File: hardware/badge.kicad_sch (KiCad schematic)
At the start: 0 parts

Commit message: add lcd sch
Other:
- added sheet lcd (lcd.kicad_sch)
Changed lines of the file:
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@@
+	)
+	(sheet
+		(at 162.56 46.99)
+		(size 29.21 26.67)
+		(fields_autoplaced yes)
+		(stroke
+			(width 0.1524)
+			(type solid)
+		)
+		(fill
+			(color 0 0 0 0.0000)
+		)
+		(property "Sheetname" "lcd"
+			(at 162.56 46.2784 0)
+			(effects
+				(font
+					(size 1.27 1.27)
+				)
+				(justify left bottom)
+			)
+		)
+		(property "Sheetfile" "lcd.kicad_sch"
+			(at 162.56 74.2446 0)
+			(effects
+				(font
+					(size 1.27 1.27)
+				)
+				(justify left top)
+			)
+		)
+		(instances
+			(project "badge"
+				(path "/dc4a3d77-b0f8-4e90-a4be-3e93c7025348"
+					(page "6")
+				)
+			)
+		)
 	)
 	(sheet

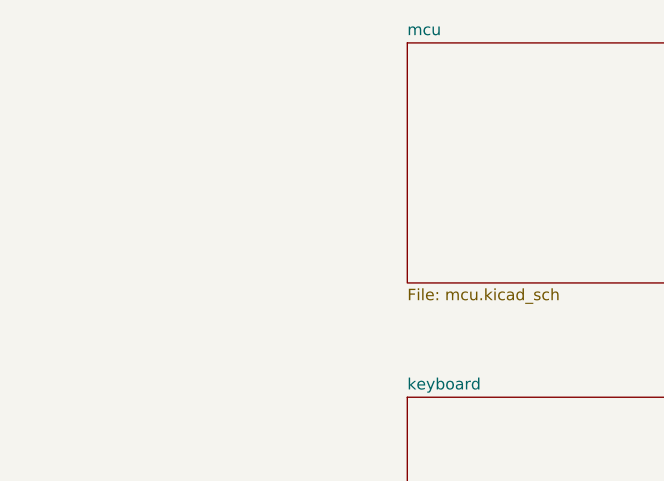
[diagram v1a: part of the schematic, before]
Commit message: remove ch340
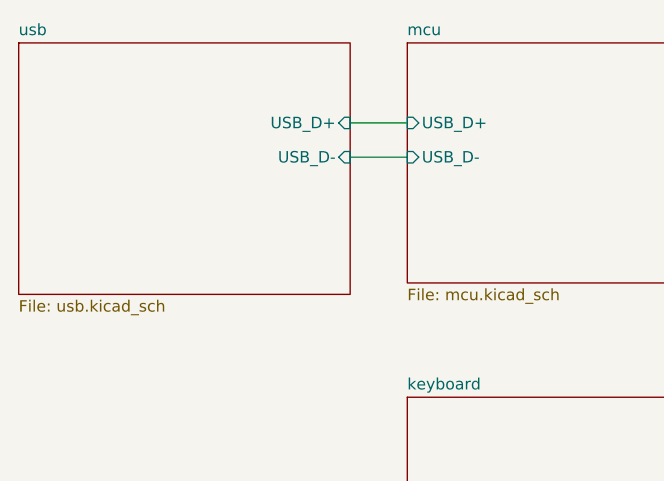
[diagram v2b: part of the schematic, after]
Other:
- added sheet usb (usb.kicad_sch)
- sheet mcu ports: added USB_D+, USB_D-; removed none
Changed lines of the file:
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@@
 	(generator_version "8.0")
 	(paper "A4")
+	(wire
+		(pts
+			(xy 71.12 59.69) (xy 77.47 59.69)
+		)
+		(stroke
+			(width 0)
+			(type default)
+		)
+	)
+	(wire
+		(pts
+			(xy 71.12 55.88) (xy 77.47 55.88)
+		)
+		(stroke
+			(width 0)
+			(type default)
+		)
+	)
+	(sheet
+		(at 34.29 46.99)
+		(size 36.83 27.94)
+		(fields_autoplaced yes)
+		(stroke
+			(width 0.1524)
+			(type solid)
+		)
+		(fill
+			(color 0 0 0 0.0000)
+		)
+		(property "Sheetname" "usb"
+			(at 34.29 46.2784 0)
+			(effects
+				(font
+					(size 1.27 1.27)
+				)
+				(justify left bottom)
+			)
+		)
+		(property "Sheetfile" "usb.kicad_sch"
+			(at 34.29 75.5146 0)
+			(effects
+				(font
+					(size 1.27 1.27)
+				)
+				(justify left top)
+			)
+		)
+		(pin "USB_D+" input
+			(at 71.12 55.88 0)
+			(effects
+				(font
+					(size 1.27 1.27)
+				)
+				(justify right)
+			)
+		)
+		(pin "USB_D-" input
+			(at 71.12 59.69 0)
+			(effects
+				(font
+					(size 1.27 1.27)
+				)
+				(justify right)
+			)
+		)
+		(instances
+			(project "badge"
+				(path "/dc4a3d77-b0f8-4e90-a4be-3e93c7025348"
+					(page "7")
+				)
+			)
+		)
+	)
 	(sheet
 		(at 77.47 86.36)
@@
 			)
 		)
+		(pin "USB_D+" input
+			(at 77.47 55.88 180)
+			(effects
+				(font
+					(size 1.27 1.27)
+				)
+				(justify left)
+			)
+		)
+		(pin "USB_D-" input
+			(at 77.47 59.69 180)
+			(effects
+				(font
+					(size 1.27 1.27)
+				)
+				(justify left)
+			)
+		)

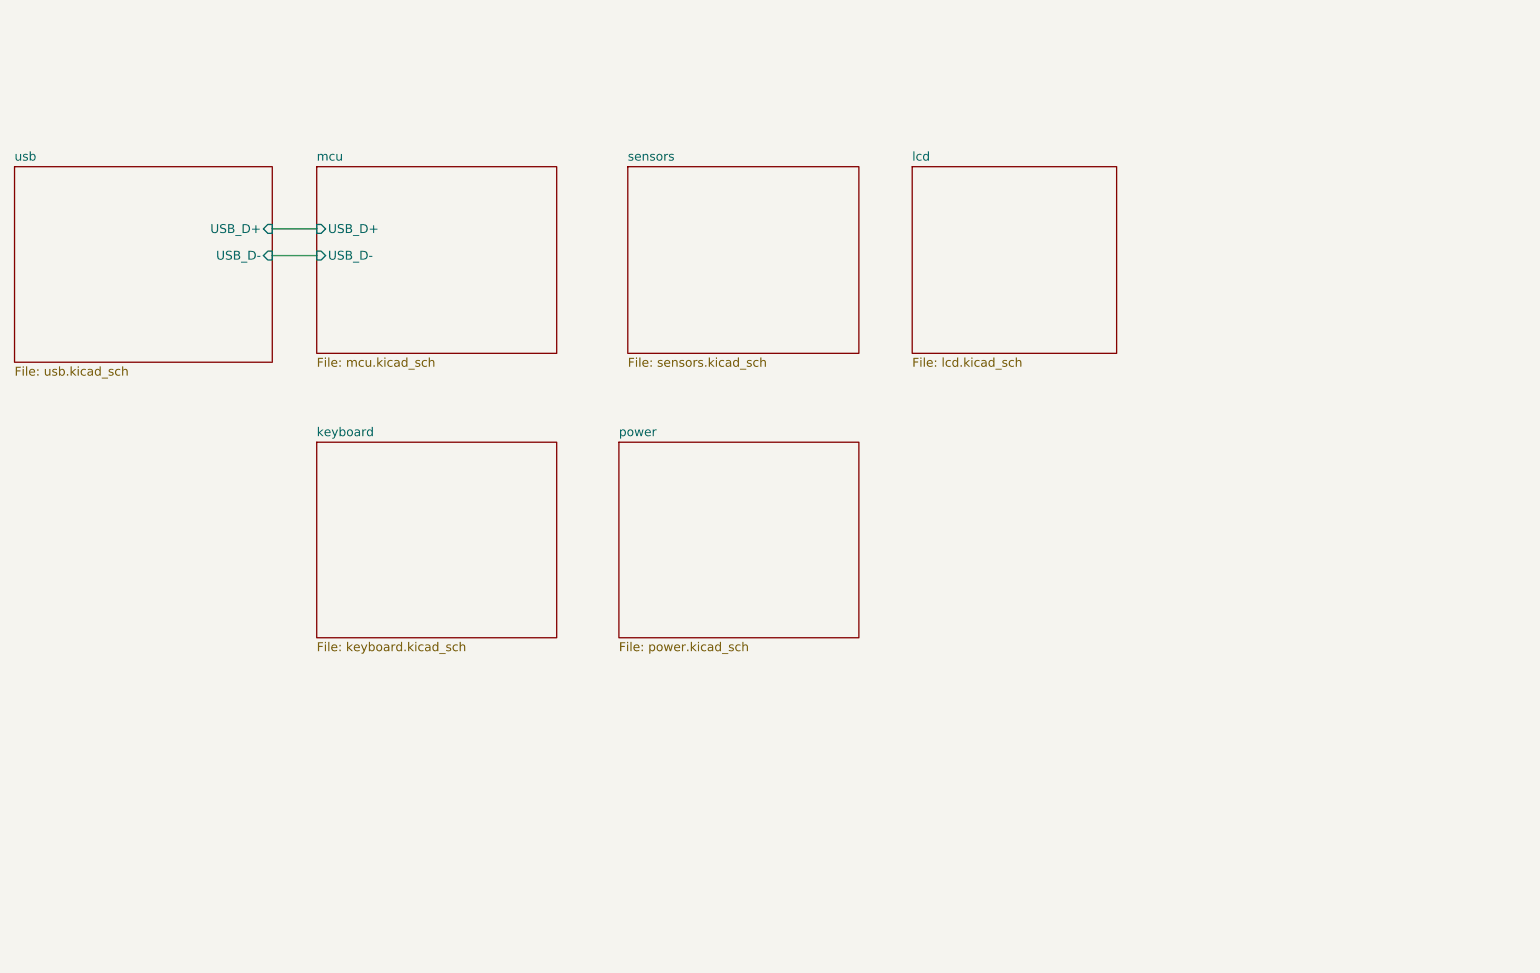
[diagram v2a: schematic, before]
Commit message: remove global labels
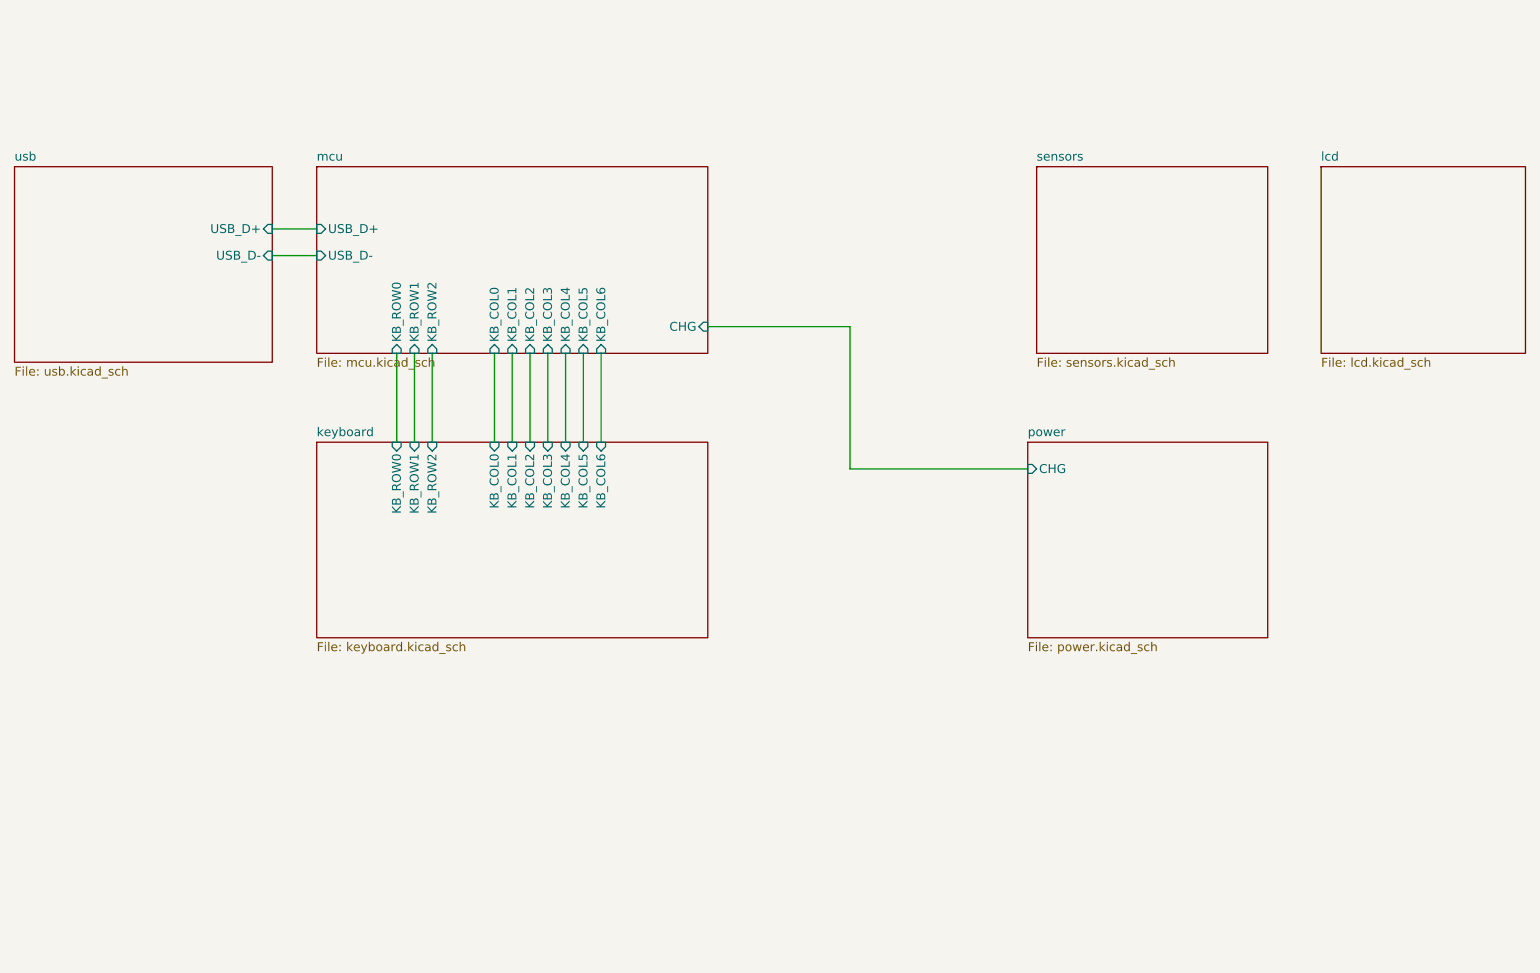
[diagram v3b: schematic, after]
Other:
- sheet keyboard ports: added KB_COL0, KB_COL1, KB_COL2, KB_COL3, KB_COL4, KB_COL5, KB_COL6, KB_ROW0, KB_ROW1, KB_ROW2; removed none
- sheet mcu ports: added CHG, KB_COL0, KB_COL1, KB_COL2, KB_COL3, KB_COL4, KB_COL5, KB_COL6, KB_ROW0, KB_ROW1, KB_ROW2; removed none
- sheet power ports: added CHG; removed none

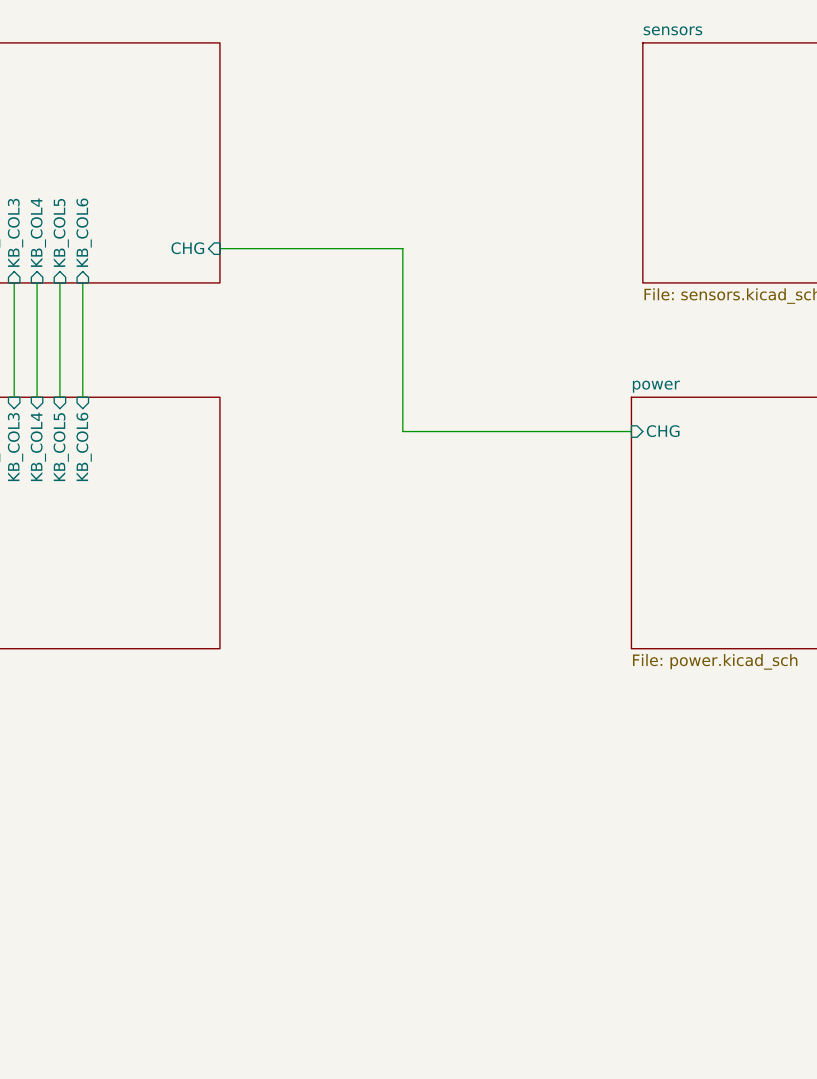
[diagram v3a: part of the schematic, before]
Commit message: add imu BMI270
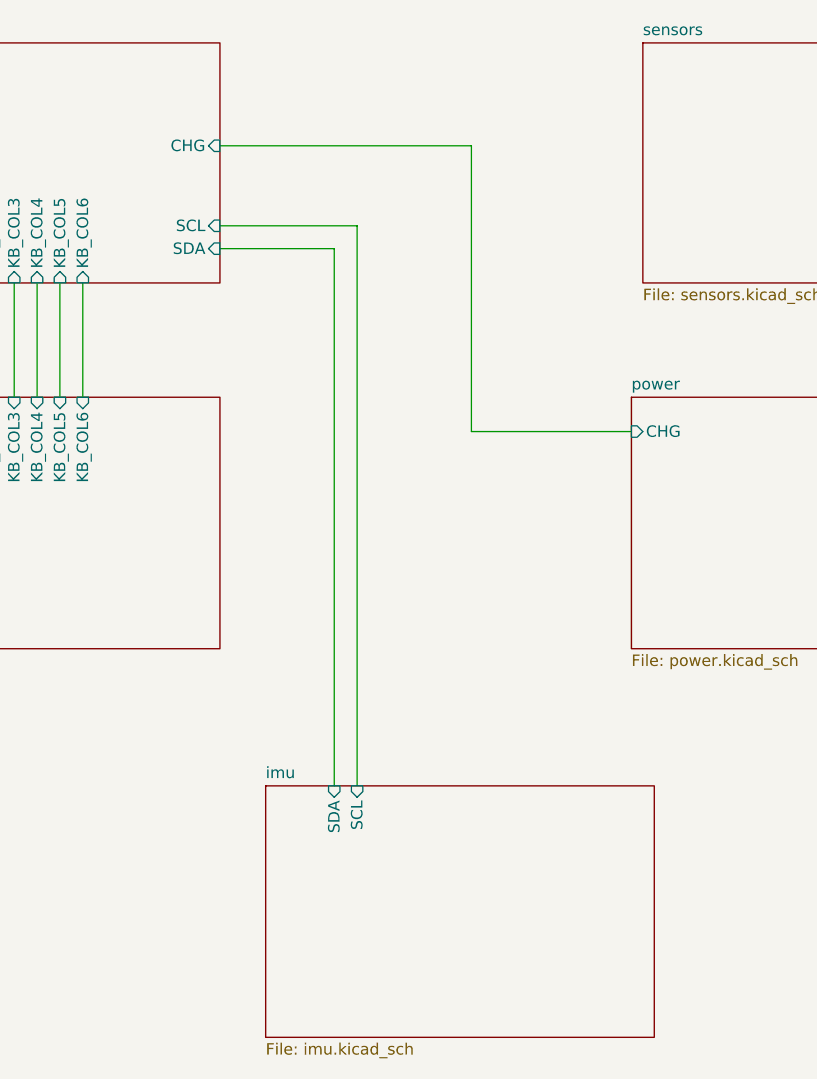
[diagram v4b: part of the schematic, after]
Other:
- added sheet imu (imu.kicad_sch)
- sheet mcu ports: added SCL, SDA; removed none
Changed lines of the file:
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@@
+	(wire
+		(pts
+			(xy 146.05 69.85) (xy 146.05 129.54)
+		)
+		(stroke
+			(width 0)
+			(type default)
+		)
+	)
 	(wire
 		(pts
@@
 	(wire
 		(pts
+			(xy 133.35 69.85) (xy 146.05 69.85)
+		)
+		(stroke
+			(width 0)
+			(type default)
+		)
+	)
+	(wire
+		(pts
+			(xy 148.59 67.31) (xy 148.59 129.54)
+		)
+		(stroke
+			(width 0)
+			(type default)
+		)
+	)
+	(wire
+		(pts
 			(xy 88.9 73.66) (xy 88.9 86.36)
 		)
@@
 	(wire
 		(pts
-			(xy 133.35 69.85) (xy 153.67 69.85)
+			(xy 133.35 67.31) (xy 148.59 67.31)
+		)
+		(stroke
+			(width 0)
+			(type default)
+		)
+	)
+	(wire
+		(pts
+			(xy 133.35 58.42) (xy 161.29 58.42)
 		)
 		(stroke
@@
 	(wire
 		(pts
-			(xy 153.67 90.17) (xy 179.07 90.17)
+			(xy 161.29 90.17) (xy 179.07 90.17)
 		)
 		(stroke
@@
 	(wire
 		(pts
-			(xy 153.67 69.85) (xy 153.67 90.17)
-		)
-		(stroke
-			(width 0)
-			(type default)
+			(xy 161.29 58.42) (xy 161.29 90.17)
+		)
+		(stroke
+			(width 0)
+			(type default)
+		)
+	)
+	(sheet
+		(at 138.43 129.54)
+		(size 43.18 27.94)
+		(fields_autoplaced yes)
+		(stroke
+			(width 0.1524)
+			(type solid)
+		)
+		(fill
+			(color 0 0 0 0.0000)
+		)
+		(property "Sheetname" "imu"
+			(at 138.43 128.8284 0)
+			(effects
+				(font
+					(size 1.27 1.27)
+				)
+				(justify left bottom)
+			)
+		)
+		(property "Sheetfile" "imu.kicad_sch"
+			(at 138.43 158.0646 0)
+			(effects
+				(font
+					(size 1.27 1.27)
+				)
+				(justify left top)
+			)
+		)
+		(pin "SDA" input
+			(at 146.05 129.54 90)
+			(effects
+				(font
+					(size 1.27 1.27)
+				)
+				(justify right)
+			)
+		)
+		(pin "SCL" input
+			(at 148.59 129.54 90)
+			(effects
+				(font
+					(size 1.27 1.27)
+				)
+				(justify right)
+			)
+		)
+		(instances
+			(project "badge"
+				(path "/dc4a3d77-b0f8-4e90-a4be-3e93c7025348"
+					(page "8")
+				)
+			)
 		)
 	)
@@
 		)
 		(pin "CHG" input
+			(at 133.35 58.42 0)
+			(effects
+				(font
+					(size 1.27 1.27)
+				)
+				(justify right)
+			)
+		)
+		(pin "SDA" input
 			(at 133.35 69.85 0)
 			(effects
 				(font
+					(size 1.27 1.27)
+				)
+				(justify right)
+			)
+		)
+		(pin "SCL" input
+			(at 133.35 67.31 0)
+			(effects
+				(font

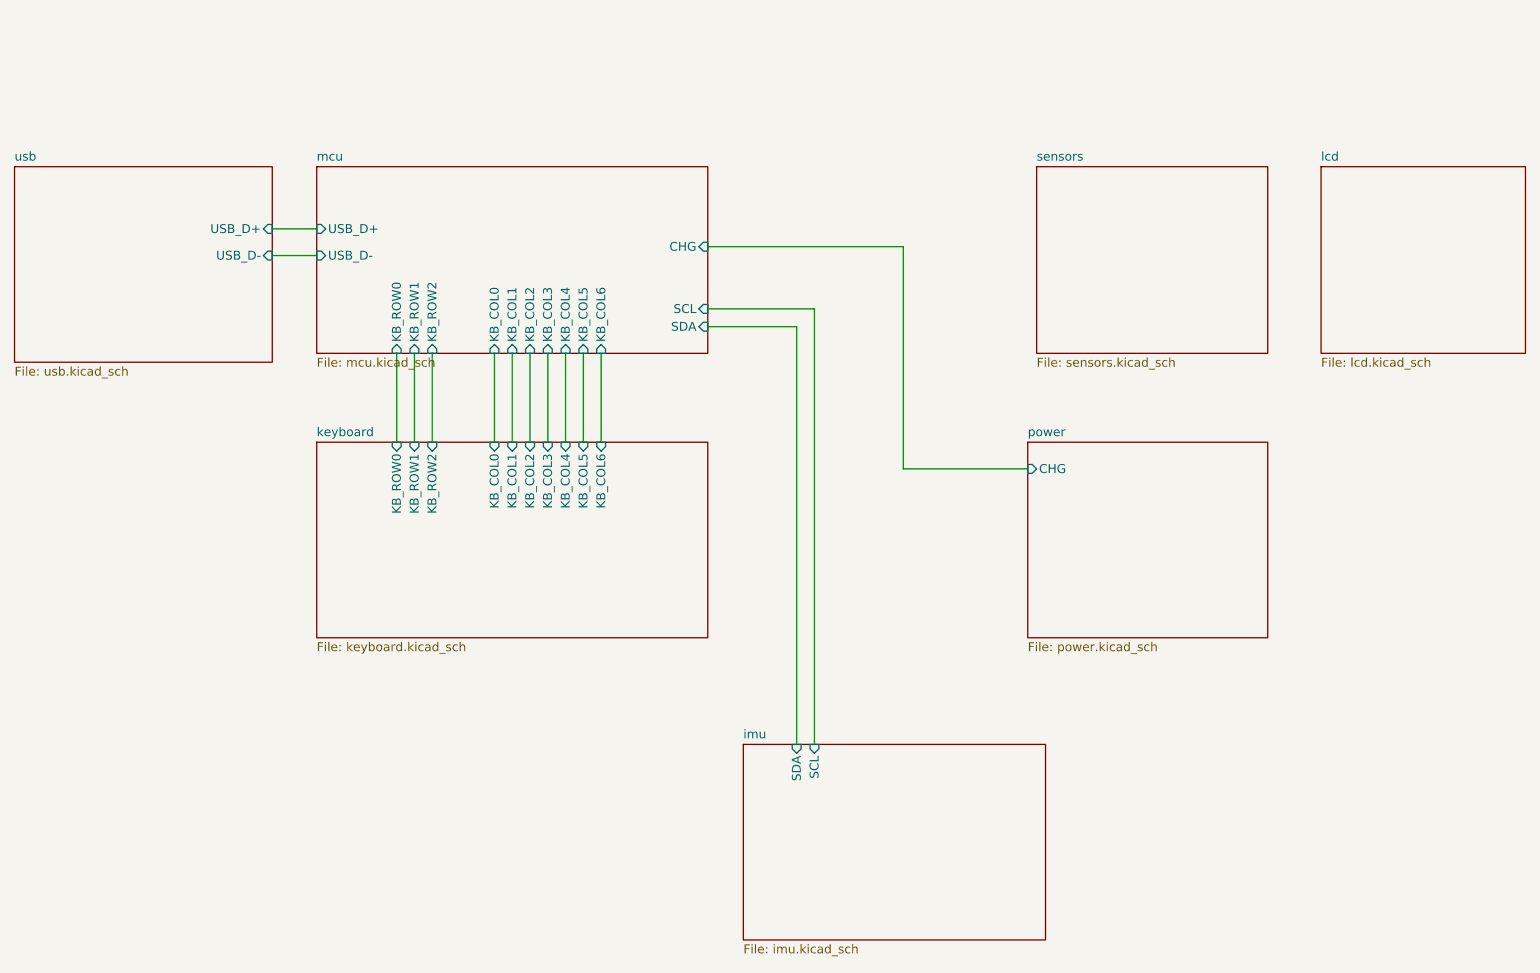
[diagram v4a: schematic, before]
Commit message: add bme280
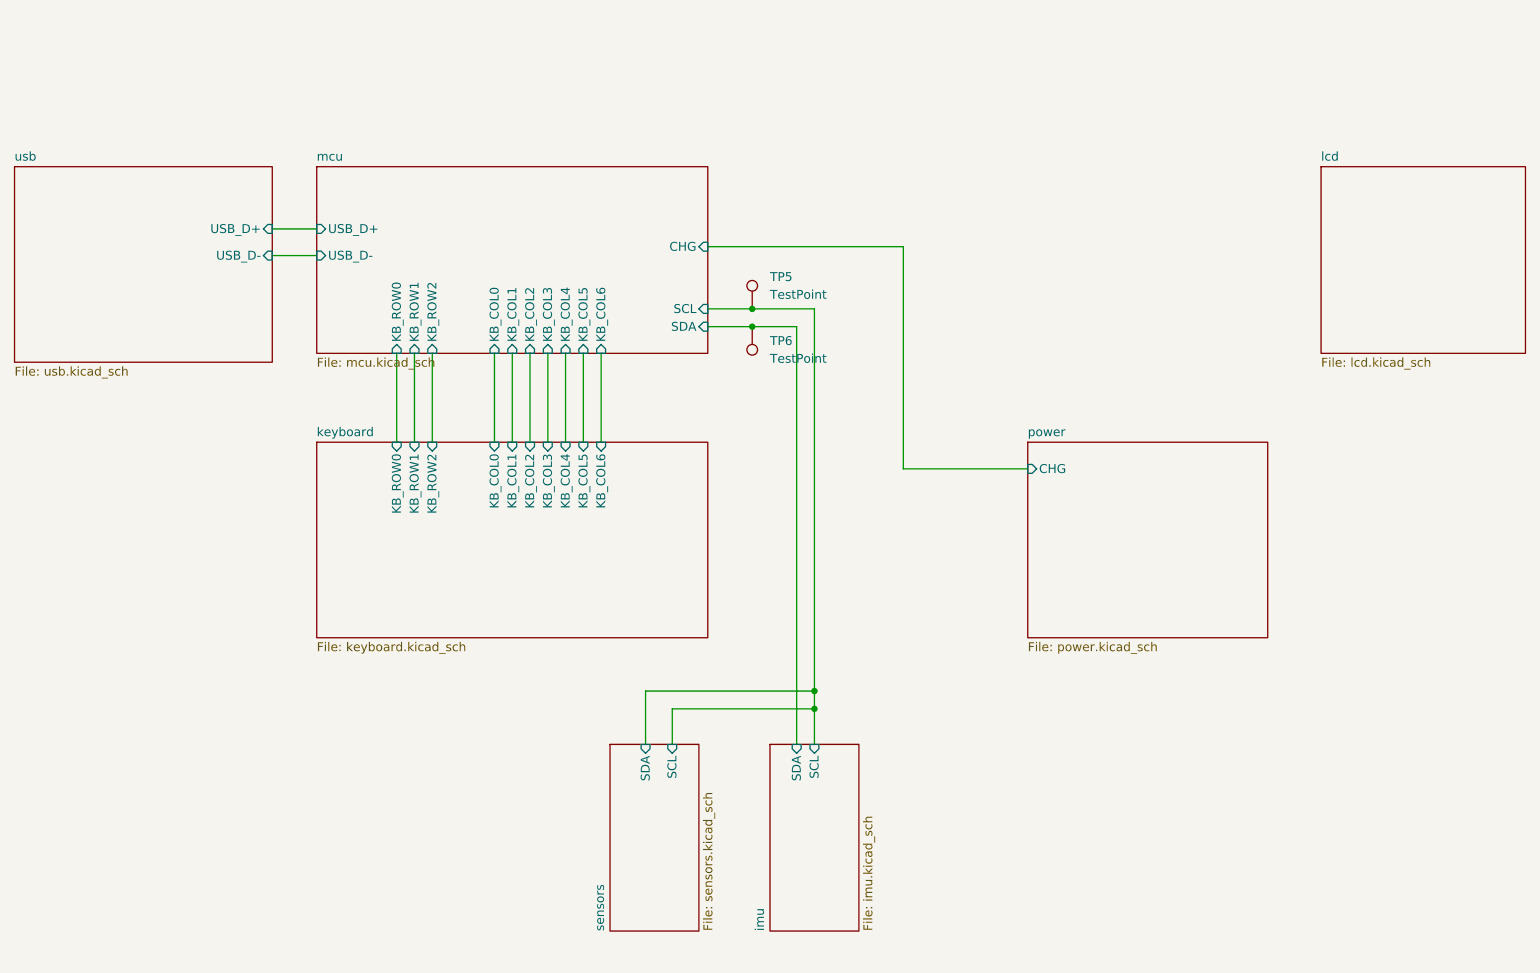
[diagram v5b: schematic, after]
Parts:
- added TP5, TP6: TestPoint, TestPoint:TestPoint_Pad_D1.0mm, symbol Connector:TestPoint
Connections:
- net imu/SCL: now also TP5.1
- net imu/SDA: now also TP6.1
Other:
- sheet sensors ports: added SCL, SDA; removed none
